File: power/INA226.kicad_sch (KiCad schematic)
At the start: 4 parts, among them U4 INA226

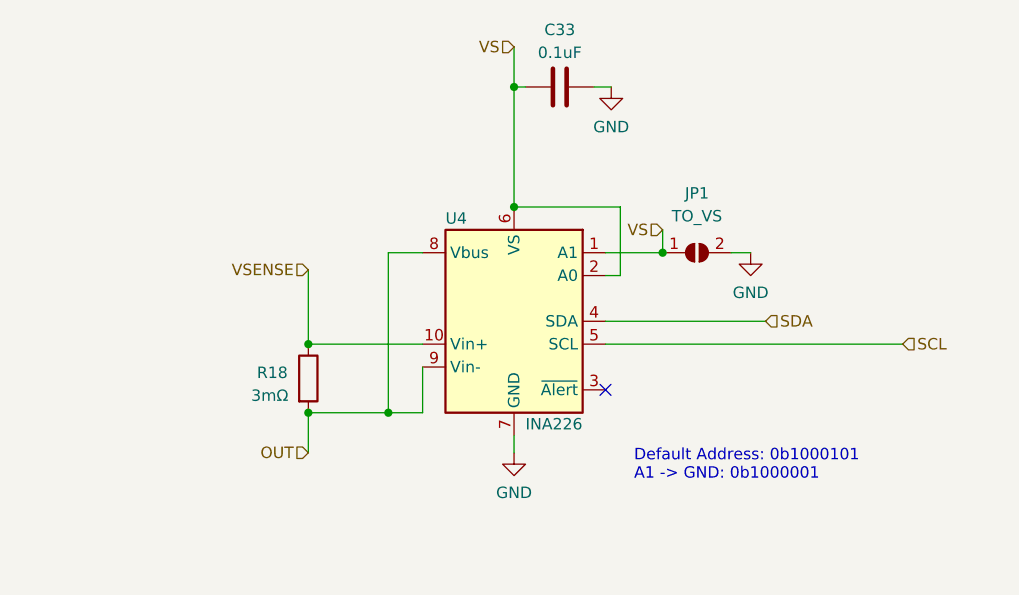
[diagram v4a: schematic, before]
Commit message: Feat: Added pull-up resistor, final silkscreen edits
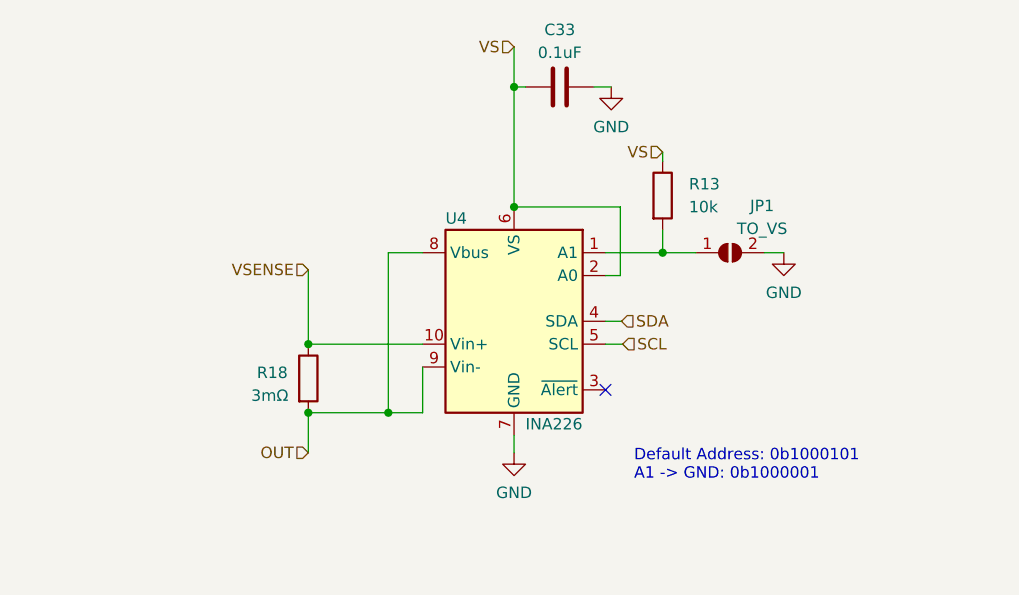
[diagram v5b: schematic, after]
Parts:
- added R13: 10k, Resistor_SMD:R_0603_1608Metric, symbol Device:R
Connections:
- net VS: now also R13.1; no longer JP1.1 (A), U4.1 (A1)
- new net: JP1.1 (A), R13.2, U4.1 (A1)
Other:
- moved on the sheet: JP1
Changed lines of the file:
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@@
   (junction (at 125.73 93.345) (diameter 0) (color 0 0 0 0)
   )
+  (junction (at 165.1 83.185) (diameter 0) (color 0 0 0 0)
+  )
   (junction (at 134.62 100.965) (diameter 0) (color 0 0 0 0)
   )
   (junction (at 125.73 100.965) (diameter 0) (color 0 0 0 0)
-  )
-  (junction (at 165.1 83.185) (diameter 0) (color 0 0 0 0)
   )
   (no_connect (at 158.75 98.425))
@@
     (stroke (width 0) (type default))
   )
-  (wire (pts (xy 158.75 93.345) (xy 191.77 93.345))
-    (stroke (width 0) (type default))
-  )
-  (wire (pts (xy 158.75 90.805) (xy 176.53 90.805))
-    (stroke (width 0) (type default))
-  )
   (wire (pts (xy 160.401 85.725) (xy 160.401 78.105))
     (stroke (width 0) (type default))
@@
     (stroke (width 0) (type default))
   )
+  (wire (pts (xy 158.75 90.805) (xy 160.528 90.805))
+    (stroke (width 0) (type default))
+  )
   (wire (pts (xy 158.75 85.725) (xy 160.401 85.725))
     (stroke (width 0) (type default))
@@
     (stroke (width 0) (type default))
   )
+  (wire (pts (xy 165.1 83.185) (xy 168.783 83.185))
+    (stroke (width 0) (type default))
+  )
   (wire (pts (xy 125.73 85.09) (xy 125.73 93.345))
     (stroke (width 0) (type default))
@@
     (stroke (width 0) (type default))
   )
-  (wire (pts (xy 172.72 83.185) (xy 174.879 83.185))
+  (wire (pts (xy 176.403 83.185) (xy 178.562 83.185))
+    (stroke (width 0) (type default))
+  )
+  (wire (pts (xy 165.1 72.009) (xy 165.1 73.025))
     (stroke (width 0) (type default))
   )
   (wire (pts (xy 158.75 83.185) (xy 165.1 83.185))
+    (stroke (width 0) (type default))
+  )
+  (wire (pts (xy 158.75 93.345) (xy 160.655 93.345))
     (stroke (width 0) (type default))
   )
@@
     (effects (font (size 1.27 1.27)) (justify right))
   )
-  (hierarchical_label "SCL" (shape input) (at 191.77 93.345 0) (fields_autoplaced)
+  (hierarchical_label "SCL" (shape input) (at 160.655 93.345 0) (fields_autoplaced)
     (effects (font (size 1.27 1.27)) (justify left))
   )
@@
     (effects (font (size 1.27 1.27)) (justify right))
   )
-  (hierarchical_label "VS" (shape input) (at 165.1 80.645 180) (fields_autoplaced)
-    (effects (font (size 1.27 1.27)) (justify right))
-  )
-  (hierarchical_label "SDA" (shape input) (at 176.53 90.805 0) (fields_autoplaced)
+  (hierarchical_label "VS" (shape input) (at 165.1 72.009 180) (fields_autoplaced)
+    (effects (font (size 1.27 1.27)) (justify right))
+  )
+  (hierarchical_label "SDA" (shape input) (at 160.528 90.805 0) (fields_autoplaced)
     (effects (font (size 1.27 1.27)) (justify left))
   )
@@
         (path "/6d3c5c52-febb-4c99-82d7-f9b22bb5762b/10807fc9-e13d-42f8-8510-6de977afc8e3"
           (reference "#PWR031") (unit 1)
+        )
+      )
+    )
+  )
+  (symbol (lib_id "Device:R") (at 165.1 76.835 0) (unit 1)
+    (in_bom yes) (on_board yes) (dnp no) (fields_autoplaced)
+    (property "Reference" "R13" (at 168.021 75.565 0)
+      (effects (font (size 1.27 1.27)) (justify left))
+    )
+    (property "Value" "10k" (at 168.021 78.105 0)
+      (effects (font (size 1.27 1.27)) (justify left))
+    )
+    (property "Footprint" "Resistor_SMD:R_0603_1608Metric" (at 163.322 76.835 90)
+      (effects (font (size 1.27 1.27)) hide)
+    )
+    (property "Datasheet" "~" (at 165.1 76.835 0)
+      (effects (font (size 1.27 1.27)) hide)
+    )
+    (pin "1")
+    (pin "2")
+    (instances
+      (project "power"
+        (path "/6d3c5c52-febb-4c99-82d7-f9b22bb5762b/10807fc9-e13d-42f8-8510-6de977afc8e3"
+          (reference "R13") (unit 1)
         )
       )
@@
     )
   )
-  (symbol (lib_id "Jumper:SolderJumper_2_Open") (at 168.91 83.185 0) (unit 1)
-    (in_bom yes) (on_board yes) (dnp no) (fields_autoplaced)
-    (property "Reference" "JP1" (at 168.91 76.581 0)
-      (effects (font (size 1.27 1.27)))
-    )
-    (property "Value" "TO_VS" (at 168.91 79.121 0)
-      (effects (font (size 1.27 1.27)))
-    )
-    (property "Footprint" "Jumper:SolderJumper-2_P1.3mm_Open_RoundedPad1.0x1.5mm" (at 168.91 83.185 0)
-      (effects (font (size 1.27 1.27)) hide)
-    )
-    (property "Datasheet" "~" (at 168.91 83.185 0)
+  (symbol (lib_id "Jumper:SolderJumper_2_Open") (at 172.593 83.185 0) (unit 1)
+    (in_bom yes) (on_board yes) (dnp no)
+    (property "Reference" "JP1" (at 176.149 77.978 0)
+      (effects (font (size 1.27 1.27)))
+    )
+    (property "Value" "TO_VS" (at 176.149 80.518 0)
+      (effects (font (size 1.27 1.27)))
+    )
+    (property "Footprint" "Jumper:SolderJumper-2_P1.3mm_Open_RoundedPad1.0x1.5mm" (at 172.593 83.185 0)
+      (effects (font (size 1.27 1.27)) hide)
+    )
+    (property "Datasheet" "~" (at 172.593 83.185 0)
       (effects (font (size 1.27 1.27)) hide)
     )
@@
     )
   )
-  (symbol (lib_id "power:GND") (at 174.879 83.185 0) (unit 1)
-    (in_bom yes) (on_board yes) (dnp no)
-    (property "Reference" "#PWR029" (at 174.879 89.535 0)
-      (effects (font (size 1.27 1.27)) hide)
-    )
-    (property "Value" "GND" (at 174.879 87.63 0)
-      (effects (font (size 1.27 1.27)))
-    )
-    (property "Footprint" "" (at 174.879 83.185 0)
-      (effects (font (size 1.27 1.27)) hide)
-    )
-    (property "Datasheet" "" (at 174.879 83.185 0)
-      (effects (font (size 1.27 1.27)) hide)
-    )
+  (symbol (lib_id "power:GND") (at 178.562 83.185 0) (unit 1)
+    (in_bom yes) (on_board yes) (dnp no)
+    (property "Reference" "#PWR029" (at 178.562 89.535 0)
+      (effects (font (size 1.27 1.27)) hide)
+    )
+    (property "Value" "GND" (at 178.562 87.63 0)
+      (effects (font (size 1.27 1.27)))
+    )
+    (property "Footprint" "" (at 178.562 83.185 0)
+      (effects (font (size 1.27 1.27)) hide)
+    )
+    (property "Datasheet" "" (at 178.562 83.185 0)
+      (effects (font (size 1.27 1.27)) hide)
+    )

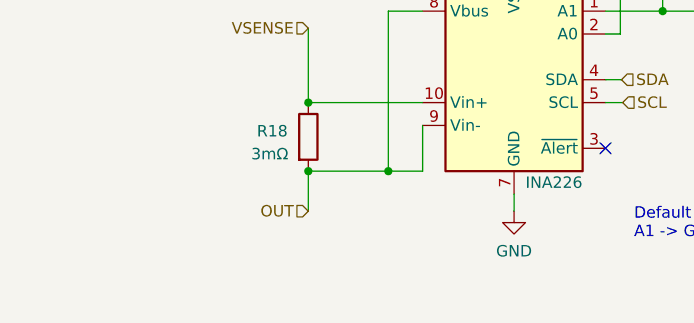
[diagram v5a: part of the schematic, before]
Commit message: Feat: Restructured labels, fixed nmos polarity, rerouted board
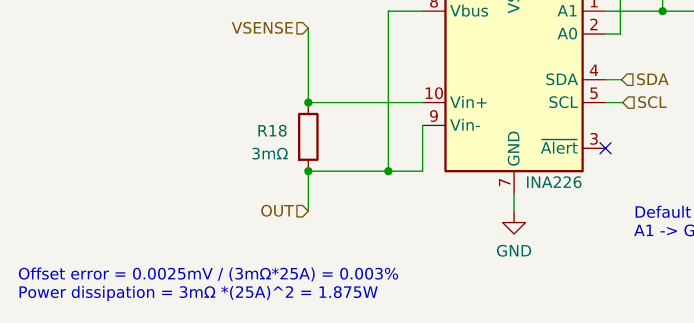
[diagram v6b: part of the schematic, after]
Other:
- note added: "Offset error = 0.0025mV / (3mΩ*25A) = 0.003% Power dissipation = 3mΩ *(25A)^2 = 1.875W"
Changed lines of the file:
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@@
     (stroke (width 0) (type default))
+  )
+  (text "Offset error = 0.0025mV / (3mΩ*25A) = 0.003%\nPower dissipation = 3mΩ *(25A)^2 = 1.875W" (exclude_from_sim no)
+    (at 93.472 115.443 0)
+    (effects (font (size 1.27 1.27)) (justify left bottom))
   )
   (text "Default Address: 0b1000101\nA1 -> GND: 0b1000001" (exclude_from_sim no)

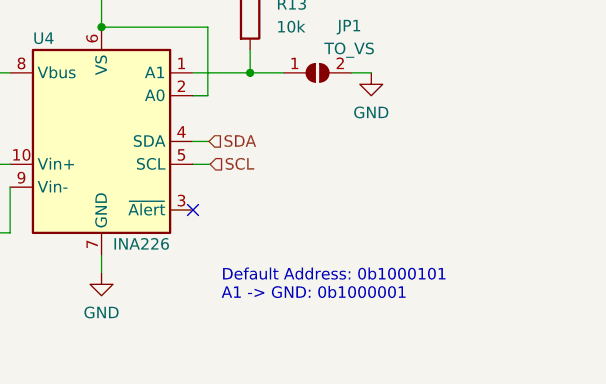
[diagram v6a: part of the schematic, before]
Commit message: Feat: Updated schematic, minor silkscreen edits
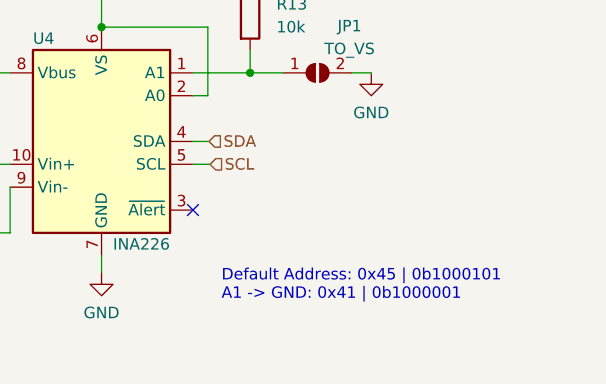
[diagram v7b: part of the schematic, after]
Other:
- note added: "Default Address: 0x45 | 0b1000101 A1 -> GND: 0x41 | 0b1000001"
- note removed: "Default Address: 0b1000101 A1 -> GND: 0b1000001"
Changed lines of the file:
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@@
     (effects (font (size 1.27 1.27)) (justify left bottom))
   )
-  (text "Default Address: 0b1000101\nA1 -> GND: 0b1000001" (exclude_from_sim no)
- (at 161.925 108.585 0)
+  (text "Default Address: 0x45 | 0b1000101\nA1 -> GND: 0x41 | 0b1000001" (exclude_from_sim no)
+    (at 161.925 108.585 0)
     (effects (font (size 1.27 1.27)) (justify left bottom))
   )

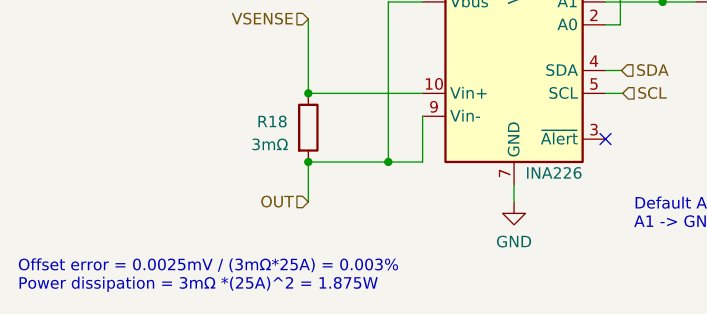
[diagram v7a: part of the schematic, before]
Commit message: Feat: Powerboard sent to chinese production
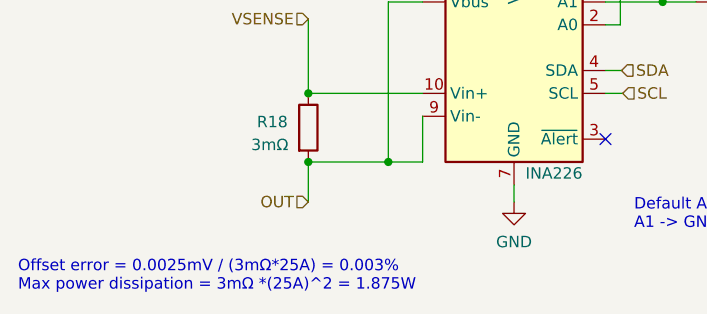
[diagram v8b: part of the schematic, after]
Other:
- note added: "Offset error = 0.0025mV / (3mΩ*25A) = 0.003% Max power dissipation = 3mΩ *(25A)^2 = 1.875W"
- note removed: "Offset error = 0.0025mV / (3mΩ*25A) = 0.003% Power dissipation = 3mΩ *(25A)^2 = 1.875W"
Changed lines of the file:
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@@
     (stroke (width 0) (type default))
   )
-  (text "Offset error = 0.0025mV / (3mΩ*25A) = 0.003%\nPower dissipation = 3mΩ *(25A)^2 = 1.875W" (exclude_from_sim no)
+  (text "Offset error = 0.0025mV / (3mΩ*25A) = 0.003%\nMax power dissipation = 3mΩ *(25A)^2 = 1.875W" (exclude_from_sim no)
     (at 93.472 115.443 0)
     (effects (font (size 1.27 1.27)) (justify left bottom))
